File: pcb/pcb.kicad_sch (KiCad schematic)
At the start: 49 parts, among them J2 ISP, SW1 Cherry MX Grey Switch w/ Gree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, SW2 Cherry MX Grey Switch w/ Gree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, SW3 1241.1100.7095, SW4 SW_SPST, U1 Display Driver, U2 Display Driver, U3 MCU, U4 Inverter, 3 Channels, U5 3:8 Demux, U6 NOR, 4 Channels, U7 OR, 2 Channels, U8 5V Buck Voltage Regulator, Y1 20MHz

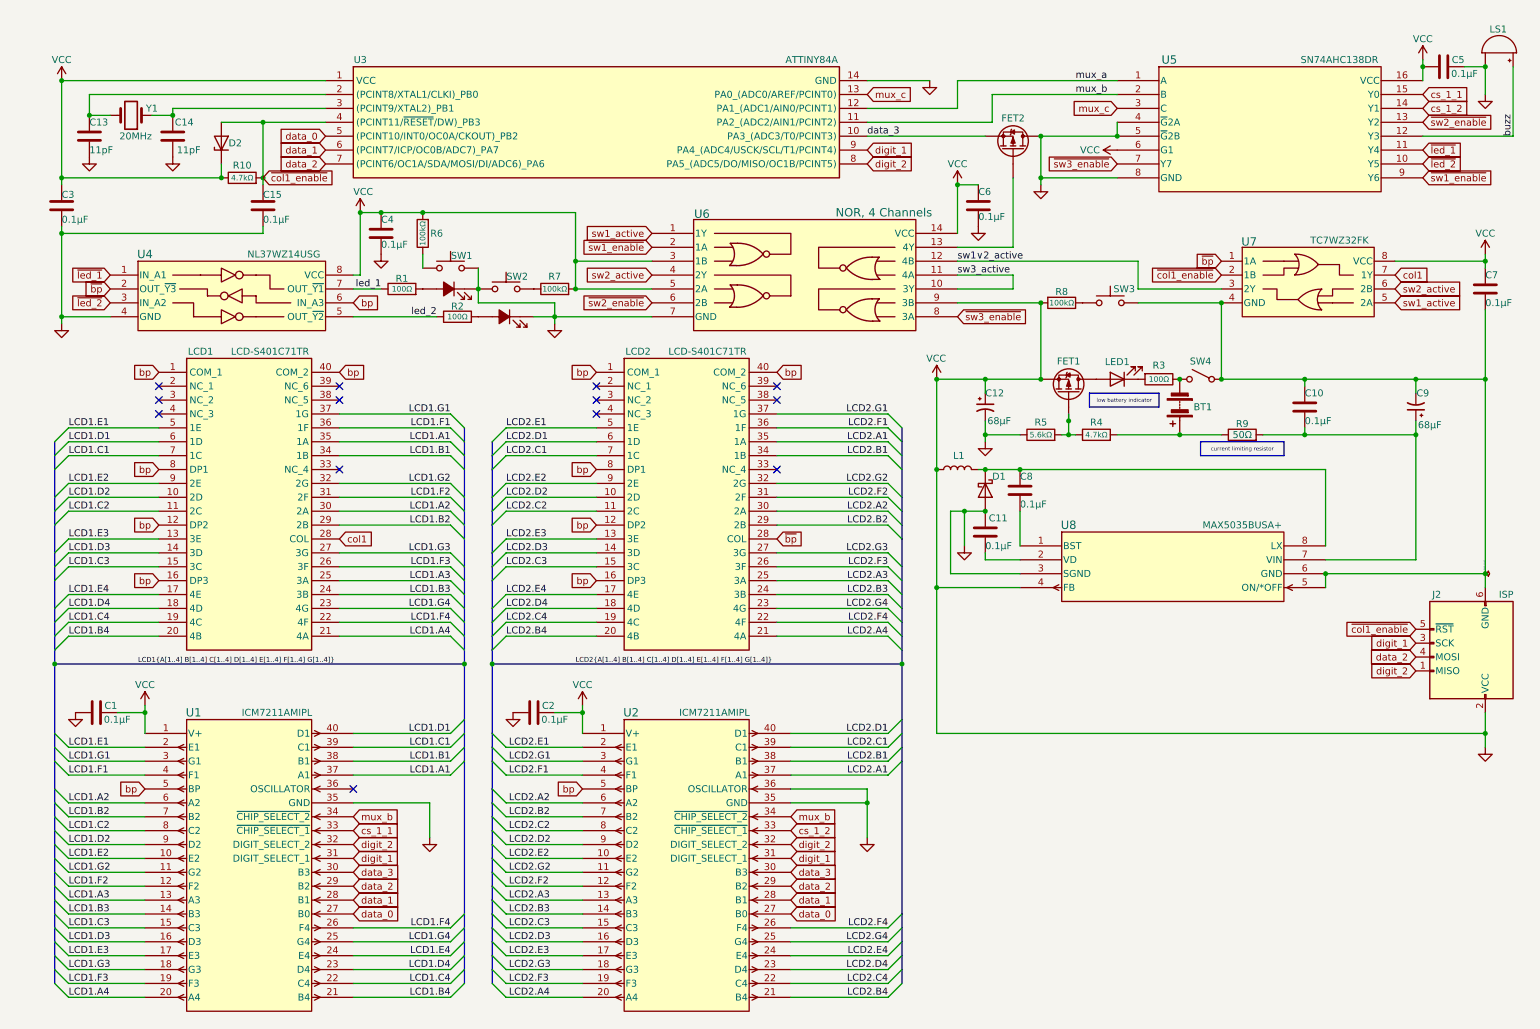
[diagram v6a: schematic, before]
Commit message: solve solder mask errors
Signed-off-by: Michael Darr <michael.e.darr@gmail.com>
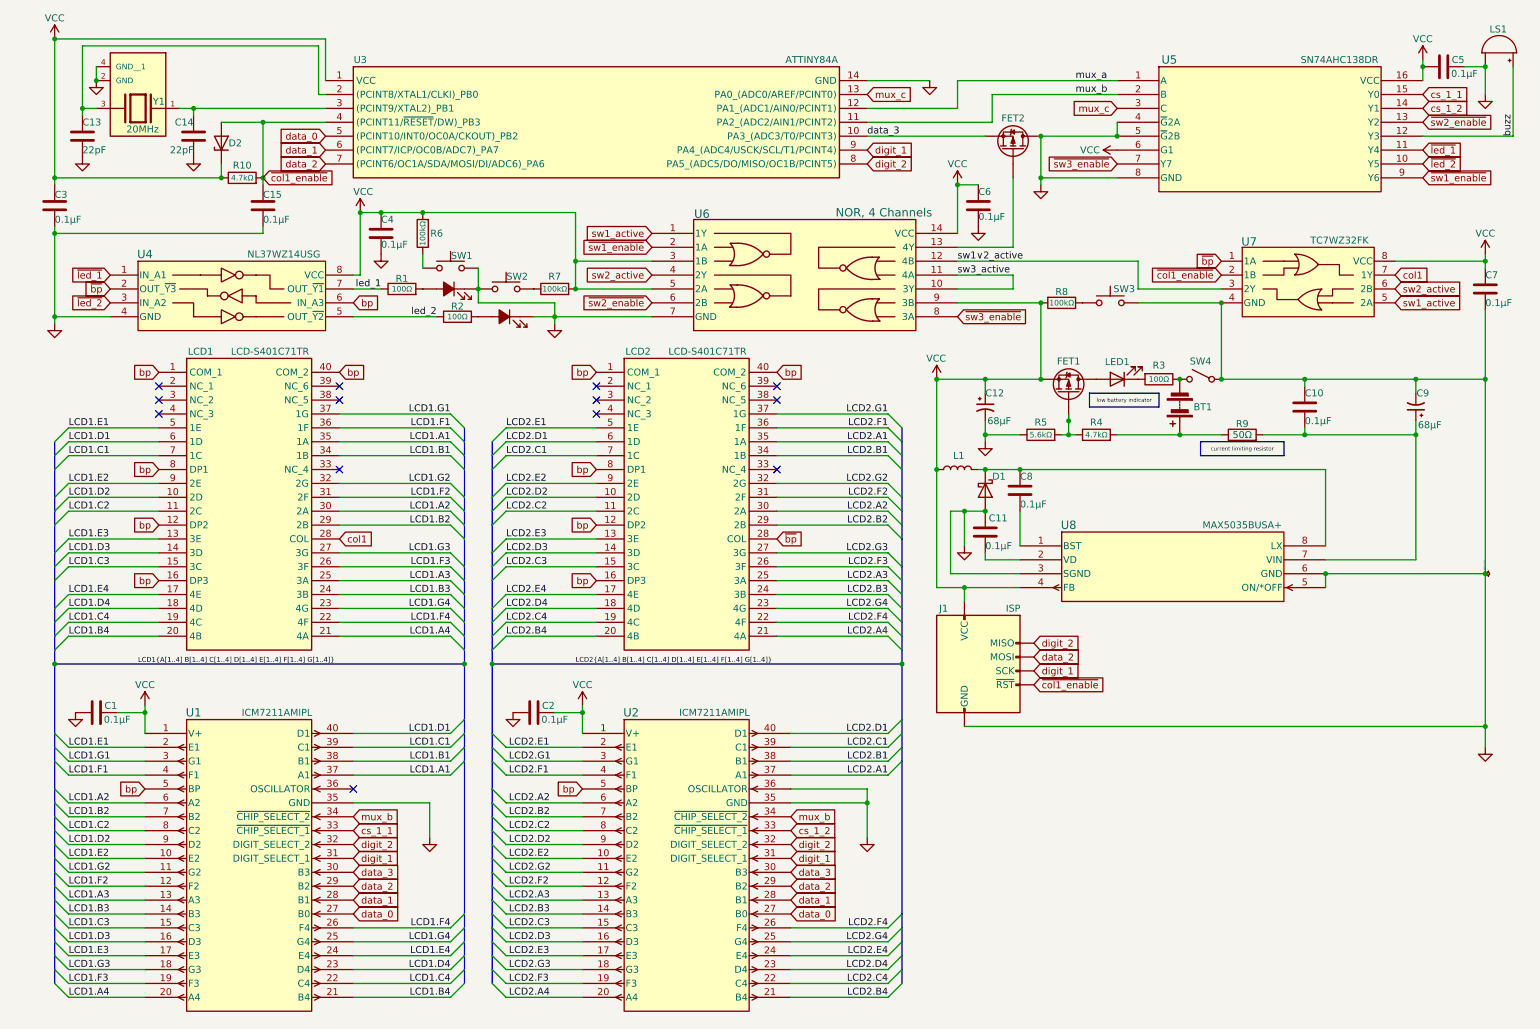
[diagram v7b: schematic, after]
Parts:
- BT1: Manufacturer_Name Memory Protection Devices, Inc -> (none)
- C1, C10, C11, C15, C2, C3, C4, C5, C6, C7, C8: footprint chess_clock:GRM033R60J104KE19D -> Capacitor_SMD:C_0805_2012Metric_Pad1.18x1.45mm_HandSolder; Manufacturer_Name Murata -> (none); Notes (none) -> 0805 package; PN GRM033R60J104KE19D -> CL21B104KBCNNNC
- C12, C9: Manufacturer_Name KYOCERA AVX -> (none)
- C13, C14: value 11pF -> 22pF; footprint chess_clock:GJM1555C1H110FB01D -> Capacitor_SMD:C_0805_2012Metric_Pad1.18x1.45mm_HandSolder; Manufacturer_Name Murata -> (none); Notes (none) -> 0805 package; PN GJM1555C1H110FB01D -> GQM2195C2E220GB12D
- D1: Manufacturer_Name Diodes Inc. -> (none)
- D2, U7: Manufacturer_Name Toshiba -> (none)
- FET1, FET2: Manufacturer_Name Yageo -> (none)
- J1: renamed from J2; Manufacturer_Name Amphenol ICC -> (none)
- L1: Manufacturer_Name Coilcraft -> (none)
- LCD1, LCD2: Manufacturer_Name Lumex -> (none)
- LED1: footprint LED_THT:LED_D3.0mm_Clear -> chess_clock:150060RS75000; Manufacturer_Name Wurth Elektronik -> (none); PN 151033RS03000 -> 150060RS75000
- LS1: Manufacturer_Name CUI Devices -> (none)
- R1, R2, R3: footprint Resistor_THT:R_Axial_DIN0204_L3.6mm_D1.6mm_P2.54mm_Vertical -> Resistor_SMD:R_0805_2012Metric_Pad1.20x1.40mm_HandSolder; Manufacturer_Name TE connectivity -> (none); Notes (none) -> 0805 package; PN ROX1SJ100R -> RC2012J101CS
- R10, R4: footprint Resistor_THT:R_Axial_DIN0204_L3.6mm_D1.6mm_P2.54mm_Vertical -> Resistor_SMD:R_0805_2012Metric_Pad1.20x1.40mm_HandSolder; Manufacturer_Name TE connectivity -> (none); Notes (none) -> 0805 package; PN CFR16J4K7 -> RC2012J472CS
- R5: footprint Resistor_THT:R_Axial_DIN0204_L3.6mm_D1.6mm_P2.54mm_Vertical -> Resistor_SMD:R_0805_2012Metric_Pad1.20x1.40mm_HandSolder; Manufacturer_Name TE connectivity -> (none); Notes (none) -> 0805 package; PN CFR50J5K6 -> RC2012J562CS
- R6, R7, R8: footprint Resistor_THT:R_Axial_DIN0204_L3.6mm_D1.6mm_P2.54mm_Vertical -> Resistor_SMD:R_0805_2012Metric_Pad1.20x1.40mm_HandSolder; Manufacturer_Name TE connectivity -> (none); Notes (none) -> 0805 package; PN ROX1SJ100K -> RC2012J104CS
- R9: Manufacturer_Name TE connectivity -> (none)
- SW1, SW2: Manufacturer_Name Cherry -> (none)
- SW3: Manufacturer_Name Schurter -> (none)
- SW4: Manufacturer_Name NKK Switches -> (none)
- U1, U2, U8: Manufacturer_Name Maxim -> (none)
- U3: Manufacturer_Name Microchip -> (none)
- U4: Manufacturer_Name Onsemi -> (none)
- U5, U6: Manufacturer_Name Texas Instruments -> (none)
- Y1: footprint chess_clock:ECS_200_18_4X_CKM -> chess_clock:ABM8-20.000MHZ-10-B1U-T; symbol Device:Crystal -> Clock-Parts:ABM8-20.000MHZ-10-B1U-T; Manufacturer_Name ECS Inc -> (none); PN ECS-200-18-4X-CKM -> ABM8-20.000MHZ-10-B1U-T
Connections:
- net GND: now also C10.1, C7.2, C9.2, J1.6 (GND), SW3.2, SW4.1 (A), U7.4 (GND), U8.5 (ON/*OFF), U8.6 (GND), Y1.2 (GND), Y1.4 (GND__1); no longer C1.2, C12.1, C2.2, C3.2, C4.1, C5.1, C6.1, C7.1, D2.1 (K), FET1.3 (S), J1.2 (VCC), L1.1, R10.1, R6.2, R7.2, R8.2, U1.1 (V+), U2.1 (V+), U3.1 (VCC), U4.8 (VCC), U5.16 (VCC), U5.6 (G1), U6.14 (VCC), U6.3 (1B), U6.5 (2A), U6.9 (3B), U7.8 (VCC), U8.4 (FB)
- net at C13.2, U3.2 ((PCINT8/XTAL1/CLKI)_PB0): now also Y1.3; no longer Y1.2
- new net VCC: C1.2, C12.1, C2.2, C3.2, C4.1, C5.1, C6.1, C7.1, D2.1 (K), FET1.3 (S), J1.2 (VCC), L1.1, R10.1, R6.2, R7.2, R8.2, U1.1 (V+), U2.1 (V+), U3.1 (VCC), U4.8 (VCC), U5.16 (VCC), U5.6 (G1), U6.14 (VCC), U6.3 (1B), U6.5 (2A), U6.9 (3B), U7.8 (VCC), U8.4 (FB)
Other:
- moved on the sheet: C13, C14, C3

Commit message: Prepare for connection
Signed-off-by: Michael Darr <michael.e.darr@gmail.com>
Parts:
- added J1, J2: Ribbon Cable Header, chess_clock:903250014, symbol Clock-Parts:903250014
- renumbered J1 to J3
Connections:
- net GND: now also J1.14, J2.14
- net VCC: now also J1.11, J2.11
- net bp: now also J1.13, J2.13
- net col1: now also J1.1, J2.1
- net cs_1_1: now also J1.12, J2.12
- net cs_1_2: now also J1.3, J2.3
- net data_0: now also J1.10, J2.10
- net data_1: now also J1.9, J2.9
- net data_2: now also J1.8, J2.8
- net data_3: now also J1.7, J2.7
- net digit_1: now also J3.1 (MISO), J1.6, J2.6; no longer J3.3 (SCK)
- net digit_2: now also J3.3 (SCK), J1.5, J2.5; no longer J3.1 (MISO)
- net mux_b: now also J1.4, J2.4
- net ~{bp}: now also J1.2, J2.2
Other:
- company: Alset -> Radish
- moved on the sheet: J3
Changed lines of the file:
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@@
     (date "2023-12-12")
     (rev "0,6")
-    (company "Alset")
+    (company "Radish")
   )
